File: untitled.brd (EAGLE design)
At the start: 100 x 80 mm, 7 parts

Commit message: finally, one via left…
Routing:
- net C0: track 98.2 -> 115.5 mm
- net D7: track 108.2 -> 113.8 mm
- net B5: track 155.2 -> 157.2 mm
- net B6: track 83.1 -> 83.9 mm
- net B3: track 121.6 -> 120.8 mm
- net C1: track 91.8 -> 92.6 mm, vias 1 -> 0
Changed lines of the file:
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@@
 <attribute name="MF" value="" x="17.78" y="7.62" size="1.778" layer="27" rot="R180" display="off"/>
 <attribute name="OC_FARNELL" value="unknown" x="17.78" y="7.62" size="1.778" layer="27" rot="R180" display="off"/>
-<attribute name="NAME" x="13.27" y="2.781" size="1.27" layer="25" ratio="10"/>
+<attribute name="NAME" x="22.02" y="2.781" size="1.27" layer="25" ratio="10"/>
 <attribute name="VALUE" x="16.51" y="10.541" size="1.27" layer="27" ratio="10" rot="R180"/>
 </element>
@@
 <contactref element="TASTENRECHTS" pad="P$2"/>
 <contactref element="U$1" pad="C0"/>
-<wire x1="15" y1="34.5" x2="12" y2="31.5" width="0.254" layer="1"/>
-<wire x1="15" y1="42.75" x2="15" y2="34.5" width="0.254" layer="1"/>
-<wire x1="16.5" y1="44.25" x2="15" y2="42.75" width="0.254" layer="1"/>
-<wire x1="18.75" y1="44.25" x2="16.5" y2="44.25" width="0.254" layer="1"/>
 <wire x1="18.75" y1="8.25" x2="18.75" y2="44.25" width="0.254" layer="1"/>
-<wire x1="12" y1="31.5" x2="11.65" y2="31.25" width="0.254" layer="1"/>
 <wire x1="18.75" y1="8.25" x2="19.05" y2="7.62" width="0.254" layer="1"/>
 <wire x1="55.5" y1="50.25" x2="58.5" y2="53.25" width="0.254" layer="16"/>
@@
 <wire x1="58.5" y1="53.25" x2="58.87" y2="53.85" width="0.254" layer="16"/>
 <via x="24.75" y="50.25" extent="1-16" drill="0.6096"/>
+<wire x1="11.65" y1="31.25" x2="12.75" y2="31.25" width="0.254" layer="1"/>
+<wire x1="12.75" y1="31.25" x2="12.75" y2="6.25" width="0.254" layer="1"/>
+<wire x1="12.75" y1="6.25" x2="13.75" y2="5" width="0.254" layer="1"/>
+<wire x1="13.75" y1="5" x2="17.5" y2="5" width="0.254" layer="1"/>
+<wire x1="17.5" y1="5" x2="18.75" y2="6.25" width="0.254" layer="1"/>
+<wire x1="18.75" y1="6.25" x2="19.05" y2="7.62" width="0.254" layer="1"/>
 </signal>
 <signal name="C1">
@@
 <contactref element="DAUMENLINKS" pad="6"/>
 <contactref element="TASTENRECHTS" pad="P$12"/>
-<wire x1="11.65" y1="43.75" x2="13.575" y2="45.675" width="0.254" layer="16"/>
-<wire x1="13.575" y1="45.675" x2="23.15" y2="55.25" width="0.254" layer="16"/>
+<wire x1="11.65" y1="43.75" x2="13.575" y2="45.675" width="0" layer="19" extent="1-16"/>
+<wire x1="11.65" y1="43.75" x2="23.15" y2="55.25" width="0.254" layer="16"/>
 <wire x1="23.15" y1="55.25" x2="47.75" y2="55.25" width="0.254" layer="16"/>
 <wire x1="47.75" y1="55.25" x2="48.89" y2="56.39" width="0.254" layer="16"/>
 <wire x1="48.89" y1="56.39" x2="58.87" y2="56.39" width="0.254" layer="16"/>
-<wire x1="16.5" y1="42.75" x2="16.5" y2="8.25" width="0.254" layer="1"/>
-<wire x1="13.575" y1="45.675" x2="16.5" y2="42.75" width="0.254" layer="16"/>
+<wire x1="16.25" y1="42.5" x2="16.25" y2="8.75" width="0.254" layer="1"/>
+<wire x1="16.25" y1="8.75" x2="16.5" y2="8.5" width="0.254" layer="1"/>
+<wire x1="16.5" y1="8.5" x2="16.5" y2="8.25" width="0.254" layer="1"/>
 <wire x1="16.5" y1="8.25" x2="16.51" y2="7.62" width="0.254" layer="1"/>
-<wire x1="13.5" y1="45.75" x2="13.575" y2="45.675" width="0.254" layer="16"/>
-<via x="16.5" y="42.75" extent="1-16" drill="0.6096"/>
+<wire x1="13.5" y1="45.75" x2="13.575" y2="45.675" width="0" layer="19" extent="1-16"/>
+<wire x1="16.25" y1="42.5" x2="15" y2="43.75" width="0.254" layer="1"/>
+<wire x1="15" y1="43.75" x2="11.65" y2="43.75" width="0.254" layer="1"/>
 </signal>
 <signal name="C3">
@@
 <contactref element="TASTENRECHTS" pad="P$1"/>
 <contactref element="U$1" pad="D6"/>
-<wire x1="24" y1="5" x2="7.5" y2="5" width="0.254" layer="16"/>
-<wire x1="24" y1="7" x2="24" y2="5" width="0.254" layer="16"/>
-<wire x1="9.75" y1="30" x2="10" y2="30" width="0.254" layer="16"/>
-<wire x1="24" y1="7" x2="24.13" y2="7.62" width="0.254" layer="16"/>
-<wire x1="7.5" y1="5" x2="7.5" y2="27.5" width="0.254" layer="16"/>
-<wire x1="7.5" y1="27.5" x2="10" y2="30" width="0.254" layer="16"/>
+<wire x1="23.75" y1="6.25" x2="21.25" y2="3.75" width="0.254" layer="16"/>
+<wire x1="21.25" y1="3.75" x2="10" y2="3.75" width="0.254" layer="16"/>
+<wire x1="10" y1="3.75" x2="7.5" y2="6.25" width="0.254" layer="16"/>
+<wire x1="23.75" y1="7.5" x2="23.75" y2="6.25" width="0.254" layer="16"/>
+<wire x1="11" y1="28.75" x2="10" y2="30" width="0" layer="19" extent="1-16"/>
+<wire x1="23.75" y1="7.5" x2="24.13" y2="7.62" width="0.254" layer="16"/>
+<wire x1="7.5" y1="6.25" x2="7.5" y2="28.75" width="0.254" layer="16"/>
+<wire x1="7.5" y1="28.75" x2="8.75" y2="30" width="0.254" layer="16"/>
+<wire x1="8.75" y1="30" x2="10" y2="30" width="0.254" layer="16"/>
 <wire x1="58.87" y1="43.69" x2="58.81" y2="43.75" width="0.254" layer="16"/>
 <wire x1="58.81" y1="43.75" x2="52.5" y2="43.75" width="0.254" layer="16"/>
@@
 <contactref element="TASTENRECHTS" pad="P$3"/>
 <contactref element="U$1" pad="D7"/>
-<wire x1="9" y1="31.5" x2="10" y2="32.5" width="0.254" layer="1"/>
-<wire x1="9" y1="12.75" x2="9" y2="31.5" width="0.254" layer="1"/>
-<wire x1="12.75" y1="9" x2="9" y2="12.75" width="0.254" layer="1"/>
-<wire x1="12.75" y1="6" x2="12.75" y2="9" width="0.254" layer="1"/>
-<wire x1="13.5" y1="5.25" x2="12.75" y2="6" width="0.254" layer="1"/>
-<wire x1="21" y1="5.25" x2="13.5" y2="5.25" width="0.254" layer="1"/>
-<wire x1="21" y1="7.5" x2="21" y2="5.25" width="0.254" layer="1"/>
-<wire x1="21" y1="7.5" x2="21.59" y2="7.62" width="0.254" layer="1"/>
+<wire x1="7.5" y1="31.25" x2="8.75" y2="32.5" width="0.254" layer="1"/>
+<wire x1="8.75" y1="32.5" x2="10" y2="32.5" width="0.254" layer="1"/>
+<wire x1="10" y1="3.75" x2="7.5" y2="6.25" width="0.254" layer="1"/>
+<wire x1="7.5" y1="6.25" x2="7.5" y2="31.25" width="0.254" layer="1"/>
+<wire x1="18.75" y1="3.75" x2="10" y2="3.75" width="0.254" layer="1"/>
+<wire x1="21.25" y1="7.5" x2="21.25" y2="6.25" width="0.254" layer="1"/>
+<wire x1="21.25" y1="6.25" x2="18.75" y2="3.75" width="0.254" layer="1"/>
+<wire x1="21.25" y1="7.5" x2="21.59" y2="7.62" width="0.254" layer="1"/>
 <wire x1="58.5" y1="46.5" x2="58.87" y2="46.23" width="0.254" layer="16"/>
 <wire x1="21.75" y1="8.25" x2="21.59" y2="7.62" width="0.254" layer="16"/>
@@
 <wire x1="8.75" y1="72.5" x2="11.65" y2="72.5" width="0.254" layer="1"/>
 <wire x1="8.75" y1="73.75" x2="10" y2="73.75" width="0.254" layer="1"/>
-<wire x1="32.25" y1="28.5" x2="12" y2="8.25" width="0.254" layer="16"/>
-<wire x1="43.5" y1="28.5" x2="32.25" y2="28.5" width="0.254" layer="16"/>
-<wire x1="12" y1="8.25" x2="11.43" y2="7.62" width="0.254" layer="16"/>
+<wire x1="31.25" y1="28.75" x2="11.25" y2="8.75" width="0.254" layer="16"/>
+<wire x1="43.5" y1="28.5" x2="42.75" y2="28.5" width="0.254" layer="16"/>
+<wire x1="42.75" y1="28.5" x2="42.5" y2="28.75" width="0.254" layer="16"/>
+<wire x1="42.5" y1="28.75" x2="31.25" y2="28.75" width="0.254" layer="16"/>
+<wire x1="11.25" y1="8.75" x2="11.43" y2="7.62" width="0.254" layer="16"/>
 <wire x1="43.5" y1="28.5" x2="43.63" y2="28.45" width="0.254" layer="16"/>
-<wire x1="40.5" y1="43.5" x2="12.5" y2="71.25" width="0.254" layer="1"/>
-<wire x1="40.5" y1="31.5" x2="40.5" y2="43.5" width="0.254" layer="1"/>
-<wire x1="43.5" y1="28.5" x2="40.5" y2="31.5" width="0.254" layer="1"/>
-<wire x1="12.5" y1="71.25" x2="11.65" y2="72.5" width="0.254" layer="1"/>
+<wire x1="40" y1="45" x2="12.5" y2="72.5" width="0.254" layer="1"/>
+<wire x1="40" y1="31.25" x2="40" y2="45" width="0.254" layer="1"/>
+<wire x1="43.5" y1="28.5" x2="42.75" y2="28.5" width="0.254" layer="1"/>
+<wire x1="42.75" y1="28.5" x2="42.5" y2="28.75" width="0.254" layer="1"/>
+<wire x1="42.5" y1="28.75" x2="40" y2="31.25" width="0.254" layer="1"/>
+<wire x1="12.5" y1="72.5" x2="11.65" y2="72.5" width="0.254" layer="1"/>
 <wire x1="43.5" y1="28.5" x2="43.63" y2="28.45" width="0.254" layer="1"/>
 </signal>
@@
 <wire x1="67.75" y1="24.5" x2="45.04" y2="24.5" width="0.254" layer="1"/>
 <wire x1="45.04" y1="24.5" x2="43.63" y2="25.91" width="0.254" layer="1"/>
-<wire x1="31.5" y1="25.5" x2="14.25" y2="8.25" width="0.254" layer="16"/>
-<wire x1="43.5" y1="25.5" x2="31.5" y2="25.5" width="0.254" layer="16"/>
-<wire x1="14.25" y1="8.25" x2="13.97" y2="7.62" width="0.254" layer="16"/>
-<wire x1="43.5" y1="25.5" x2="43.63" y2="25.91" width="0.254" layer="16"/>
+<wire x1="31.25" y1="26.25" x2="13.75" y2="8.75" width="0.254" layer="16"/>
+<wire x1="42.25" y1="26.25" x2="31.25" y2="26.25" width="0.254" layer="16"/>
+<wire x1="13.75" y1="8.75" x2="13.97" y2="7.62" width="0.254" layer="16"/>
+<wire x1="42.25" y1="26.25" x2="43.63" y2="25.91" width="0.254" layer="16"/>
 </signal>
 <signal name="D0">
@@
 <wire x1="15" y1="67.5" x2="15" y2="58.75" width="0.254" layer="1"/>
 <wire x1="15" y1="58.75" x2="6.25" y2="50" width="0.254" layer="1"/>
-<wire x1="6.25" y1="50" x2="6.25" y2="38.75" width="0.254" layer="1"/>
-<wire x1="6.25" y1="38.75" x2="7.5" y2="37.5" width="0.254" layer="1"/>
-<wire x1="7.5" y1="37.5" x2="10" y2="37.5" width="0.254" layer="1"/>
+<wire x1="6.25" y1="50" x2="6.25" y2="40" width="0.254" layer="1"/>
+<wire x1="6.25" y1="40" x2="8.75" y2="37.5" width="0.254" layer="1"/>
+<wire x1="8.75" y1="37.5" x2="10" y2="37.5" width="0.254" layer="1"/>
 <wire x1="10" y1="37.5" x2="39.66" y2="37.5" width="0.254" layer="16"/>
 <wire x1="39.66" y1="37.5" x2="43.63" y2="33.53" width="0.254" layer="16"/>

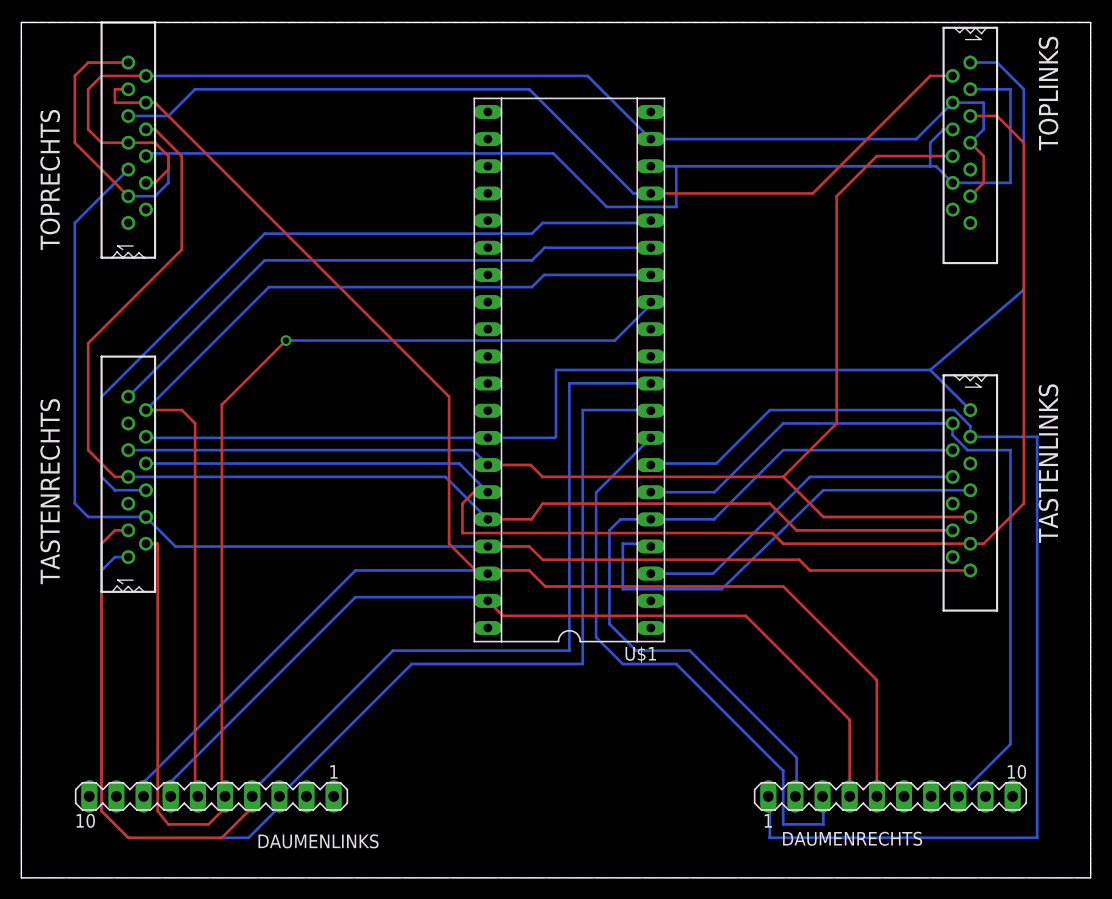
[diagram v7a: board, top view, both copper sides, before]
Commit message: some more connector cleanup
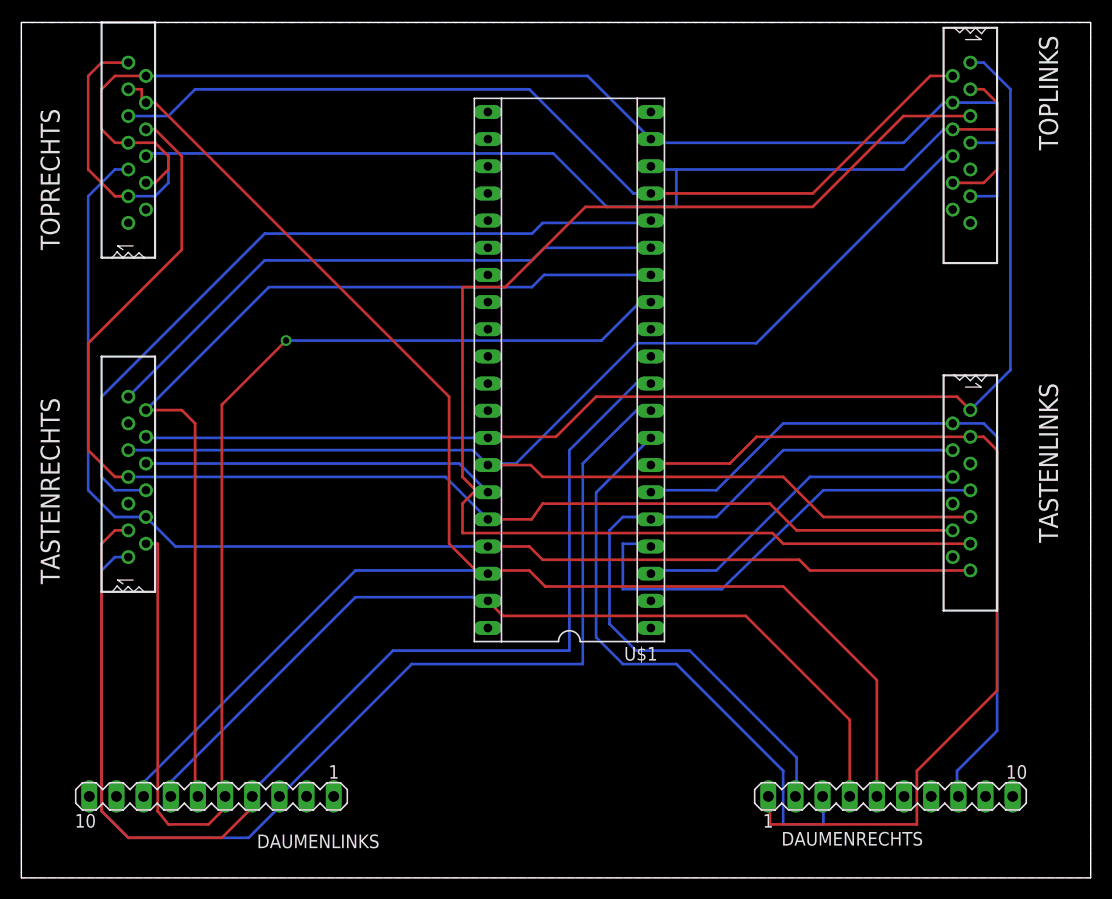
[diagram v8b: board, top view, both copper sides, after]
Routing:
- net B2: track 133.1 -> 160.4 mm
- net D4: track 106.5 -> 88.7 mm
- net B1: track 122.1 -> 136.8 mm
- net B0: track 121.3 -> 115.6 mm
- net C5: track 132.9 -> 127.9 mm
- net D7: track 113.8 -> 109.9 mm
- net D6: track 109.1 -> 106.2 mm
- net B5: track 157.2 -> 154.7 mm
- net C6: track 114.6 -> 117.1 mm
- net B4: track 119.7 -> 117.9 mm
- net D3: track 72.4 -> 70.8 mm
- net D1: track 43.8 -> 43.2 mm
